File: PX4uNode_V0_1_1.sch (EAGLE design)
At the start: 131 parts, among them M3_MOUNT1101 MOUNT-HOLE3.1MM, M3_MOUNT1102 MOUNT-HOLE3.1MM, M3_MOUNT1103 MOUNT-HOLE3.1MM, M3_MOUNT1104 MOUNT-HOLE3.1MM, U101 STM32F4X7VX, U401 MAX3051, U402 MAX3051, X101 3.2x2.5 mm / 24 MHz / 15 ppm

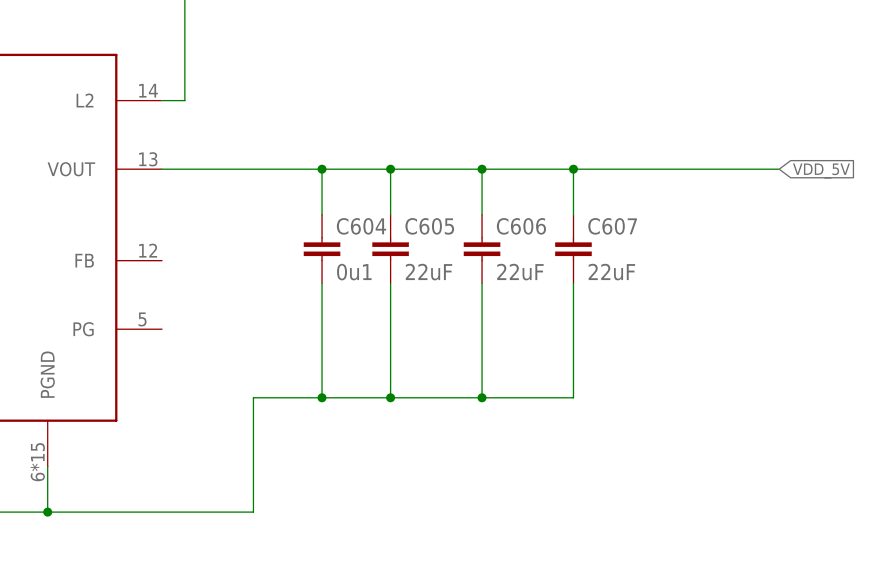
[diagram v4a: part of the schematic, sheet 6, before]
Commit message: uNode - CAN river 3V3 connected
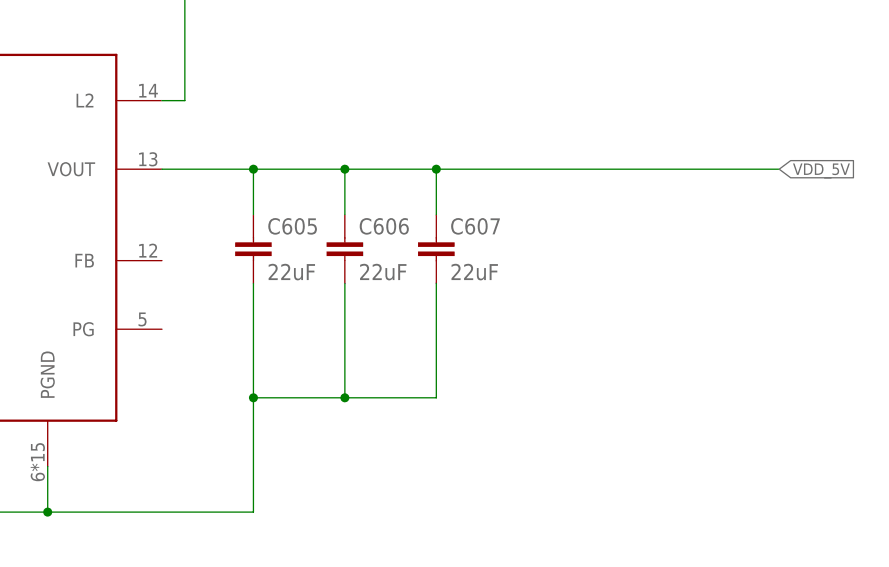
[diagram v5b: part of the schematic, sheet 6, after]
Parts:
- removed C604: 0u1, pixhawk2:CAP0402
- removed JP702: M01SMD-4.5X1.5, SparkFun-Connectors:M01SMD-4.5X1.5
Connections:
- net GND: no longer C604.2, JP702.1
- net VDD_5V: no longer C604.1
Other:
- moved on the sheet: C605, C606, C607
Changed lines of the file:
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@@
-<attribute name="PARTNO" value="CC0402ZRY5V7BB104"/>
-</part>
-<part name="C604" library="pixhawk2" deviceset="CAP" device="0402" value="0u1">
 <attribute name="PARTNO" value="CC0402ZRY5V7BB104"/>
 </part>
@@
 <part name="R1002" library="pixhawk2" deviceset="RESISTOR" device="0402-RES" value="220R">
 <attribute name="PARTNO" value="RC0402FR-07220RL"/>
-</part>
-<part name="JP702" library="SparkFun-Connectors" deviceset="M01" device="SMD-4.5X1.5">
-<attribute name="BOM" value="EXCLUDE"/>
 </part>
 <part name="JP5" library="SparkFun-Connectors" deviceset="M04" device="PTH"/>
@@
 </instance>
 <instance part="SUPPLY2" gate="GND" x="91.44" y="66.04"/>
-<instance part="C607" gate="G$1" x="167.64" y="111.76"/>
-<instance part="C605" gate="G$1" x="147.32" y="111.76"/>
-<instance part="C606" gate="G$1" x="157.48" y="111.76"/>
+<instance part="C607" gate="G$1" x="152.4" y="111.76"/>
+<instance part="C605" gate="G$1" x="132.08" y="111.76"/>
+<instance part="C606" gate="G$1" x="142.24" y="111.76"/>
 <instance part="C601" gate="G$1" x="50.8" y="104.14"/>
 <instance part="C603" gate="G$1" x="68.58" y="93.98">
 <attribute name="PARTNO" x="68.58" y="93.98" size="1.778" layer="96" display="off"/>
-</instance>
-<instance part="C604" gate="G$1" x="139.7" y="111.76">
-<attribute name="PARTNO" x="139.7" y="111.76" size="1.778" layer="96" display="off"/>
 </instance>
 <instance part="C602" gate="G$1" x="60.96" y="104.14">
@@
 <wire x1="109.22" y1="83.82" x2="132.08" y2="83.82" width="0.1524" layer="91"/>
 <wire x1="132.08" y1="83.82" x2="132.08" y2="96.52" width="0.1524" layer="91"/>
-<wire x1="132.08" y1="96.52" x2="139.7" y2="96.52" width="0.1524" layer="91"/>
-<wire x1="139.7" y1="96.52" x2="147.32" y2="96.52" width="0.1524" layer="91"/>
-<wire x1="147.32" y1="96.52" x2="157.48" y2="96.52" width="0.1524" layer="91"/>
-<wire x1="157.48" y1="96.52" x2="167.64" y2="96.52" width="0.1524" layer="91"/>
-<wire x1="167.64" y1="96.52" x2="167.64" y2="109.22" width="0.1524" layer="91"/>
+<wire x1="132.08" y1="96.52" x2="142.24" y2="96.52" width="0.1524" layer="91"/>
+<wire x1="142.24" y1="96.52" x2="152.4" y2="96.52" width="0.1524" layer="91"/>
+<wire x1="152.4" y1="96.52" x2="152.4" y2="109.22" width="0.1524" layer="91"/>
 <pinref part="C606" gate="G$1" pin="2"/>
-<wire x1="157.48" y1="109.22" x2="157.48" y2="96.52" width="0.1524" layer="91"/>
+<wire x1="142.24" y1="109.22" x2="142.24" y2="96.52" width="0.1524" layer="91"/>
 <pinref part="C605" gate="G$1" pin="2"/>
-<wire x1="147.32" y1="109.22" x2="147.32" y2="96.52" width="0.1524" layer="91"/>
-<junction x="147.32" y="96.52"/>
-<junction x="157.48" y="96.52"/>
+<wire x1="132.08" y1="109.22" x2="132.08" y2="96.52" width="0.1524" layer="91"/>
+<junction x="132.08" y="96.52"/>
+<junction x="142.24" y="96.52"/>
 <pinref part="C601" gate="G$1" pin="2"/>
 <junction x="109.22" y="83.82"/>
@@
 <wire x1="68.58" y1="73.66" x2="76.2" y2="73.66" width="0.1524" layer="91"/>
 <junction x="76.2" y="73.66"/>
-<pinref part="C604" gate="G$1" pin="2"/>
-<wire x1="139.7" y1="109.22" x2="139.7" y2="96.52" width="0.1524" layer="91"/>
-<junction x="139.7" y="96.52"/>
 <pinref part="C602" gate="G$1" pin="2"/>
 <wire x1="60.96" y1="101.6" x2="60.96" y2="83.82" width="0.1524" layer="91"/>
@@
 <pinref part="U$601" gate="A" pin="VOUT"/>
 <pinref part="C607" gate="G$1" pin="1"/>
-<wire x1="121.92" y1="121.92" x2="139.7" y2="121.92" width="0.1524" layer="91"/>
-<wire x1="139.7" y1="121.92" x2="147.32" y2="121.92" width="0.1524" layer="91"/>
-<wire x1="147.32" y1="121.92" x2="157.48" y2="121.92" width="0.1524" layer="91"/>
-<wire x1="157.48" y1="121.92" x2="167.64" y2="121.92" width="0.1524" layer="91"/>
-<wire x1="167.64" y1="121.92" x2="167.64" y2="116.84" width="0.1524" layer="91"/>
+<wire x1="121.92" y1="121.92" x2="132.08" y2="121.92" width="0.1524" layer="91"/>
+<wire x1="132.08" y1="121.92" x2="142.24" y2="121.92" width="0.1524" layer="91"/>
+<wire x1="142.24" y1="121.92" x2="152.4" y2="121.92" width="0.1524" layer="91"/>
+<wire x1="152.4" y1="121.92" x2="152.4" y2="116.84" width="0.1524" layer="91"/>
 <pinref part="C606" gate="G$1" pin="1"/>
-<wire x1="157.48" y1="116.84" x2="157.48" y2="121.92" width="0.1524" layer="91"/>
+<wire x1="142.24" y1="116.84" x2="142.24" y2="121.92" width="0.1524" layer="91"/>
 <pinref part="C605" gate="G$1" pin="1"/>
-<wire x1="147.32" y1="116.84" x2="147.32" y2="121.92" width="0.1524" layer="91"/>
-<wire x1="167.64" y1="121.92" x2="190.5" y2="121.92" width="0.1524" layer="91"/>
+<wire x1="132.08" y1="116.84" x2="132.08" y2="121.92" width="0.1524" layer="91"/>
+<wire x1="152.4" y1="121.92" x2="190.5" y2="121.92" width="0.1524" layer="91"/>
 <label x="190.5" y="121.92" size="1.27" layer="95" xref="yes"/>
-<junction x="167.64" y="121.92"/>
-<junction x="147.32" y="121.92"/>
-<junction x="157.48" y="121.92"/>
-<pinref part="C604" gate="G$1" pin="1"/>
-<wire x1="139.7" y1="116.84" x2="139.7" y2="121.92" width="0.1524" layer="91"/>
-<junction x="139.7" y="121.92"/>
+<junction x="152.4" y="121.92"/>
+<junction x="132.08" y="121.92"/>
+<junction x="142.24" y="121.92"/>
 </segment>
 </net>
@@
 <instance part="C710" gate="G$1" x="170.18" y="157.48">
 <attribute name="PARTNO" x="170.18" y="157.48" size="1.778" layer="96" display="off"/>
-</instance>
-<instance part="JP702" gate="G$1" x="195.58" y="91.44">
-<attribute name="BOM" x="195.58" y="91.44" size="1.778" layer="96" display="off"/>
 </instance>
 <instance part="D2" gate="G$1" x="205.74" y="127" rot="R270"/>
@@
 <wire x1="233.68" y1="91.44" x2="233.68" y2="96.52" width="0.1524" layer="91"/>
 <junction x="223.52" y="91.44"/>
-<pinref part="JP702" gate="G$1" pin="1"/>
-<wire x1="203.2" y1="91.44" x2="223.52" y2="91.44" width="0.1524" layer="91"/>
-</segment>
-<segment>
+</segment>
+<segment>
